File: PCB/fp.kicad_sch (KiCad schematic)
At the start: 29 parts, among them J1 Line Out

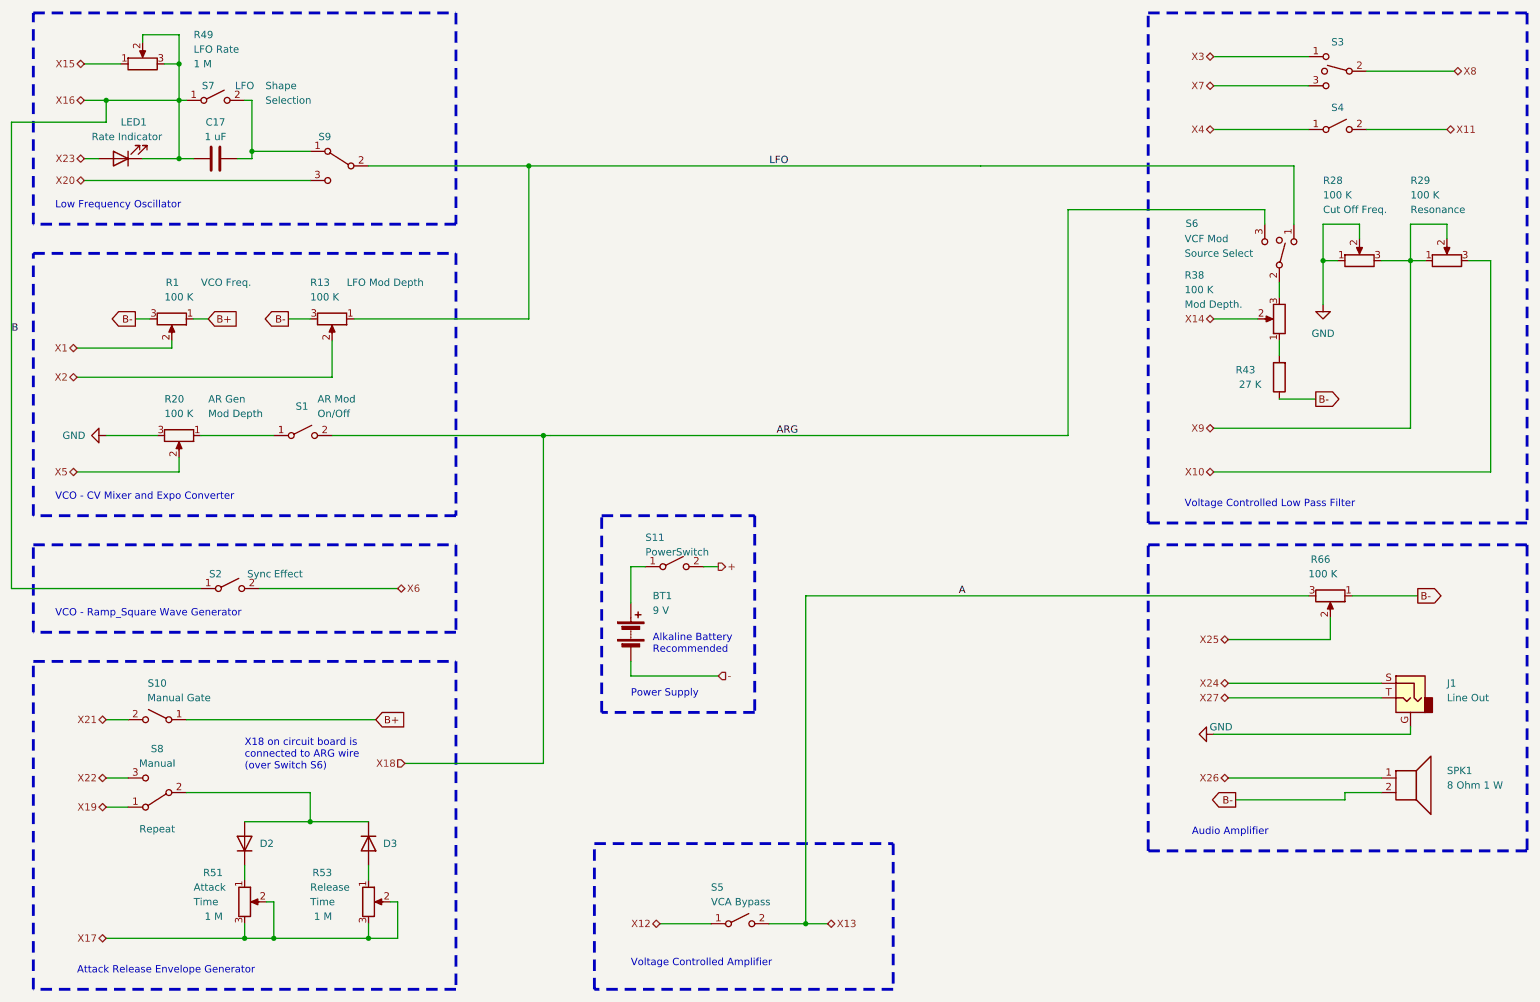
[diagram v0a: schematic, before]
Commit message: Change TO-92 transistors to wide package to avoid shorting during soldering
Added B- hole for speaker
Added more vias to shorten traces
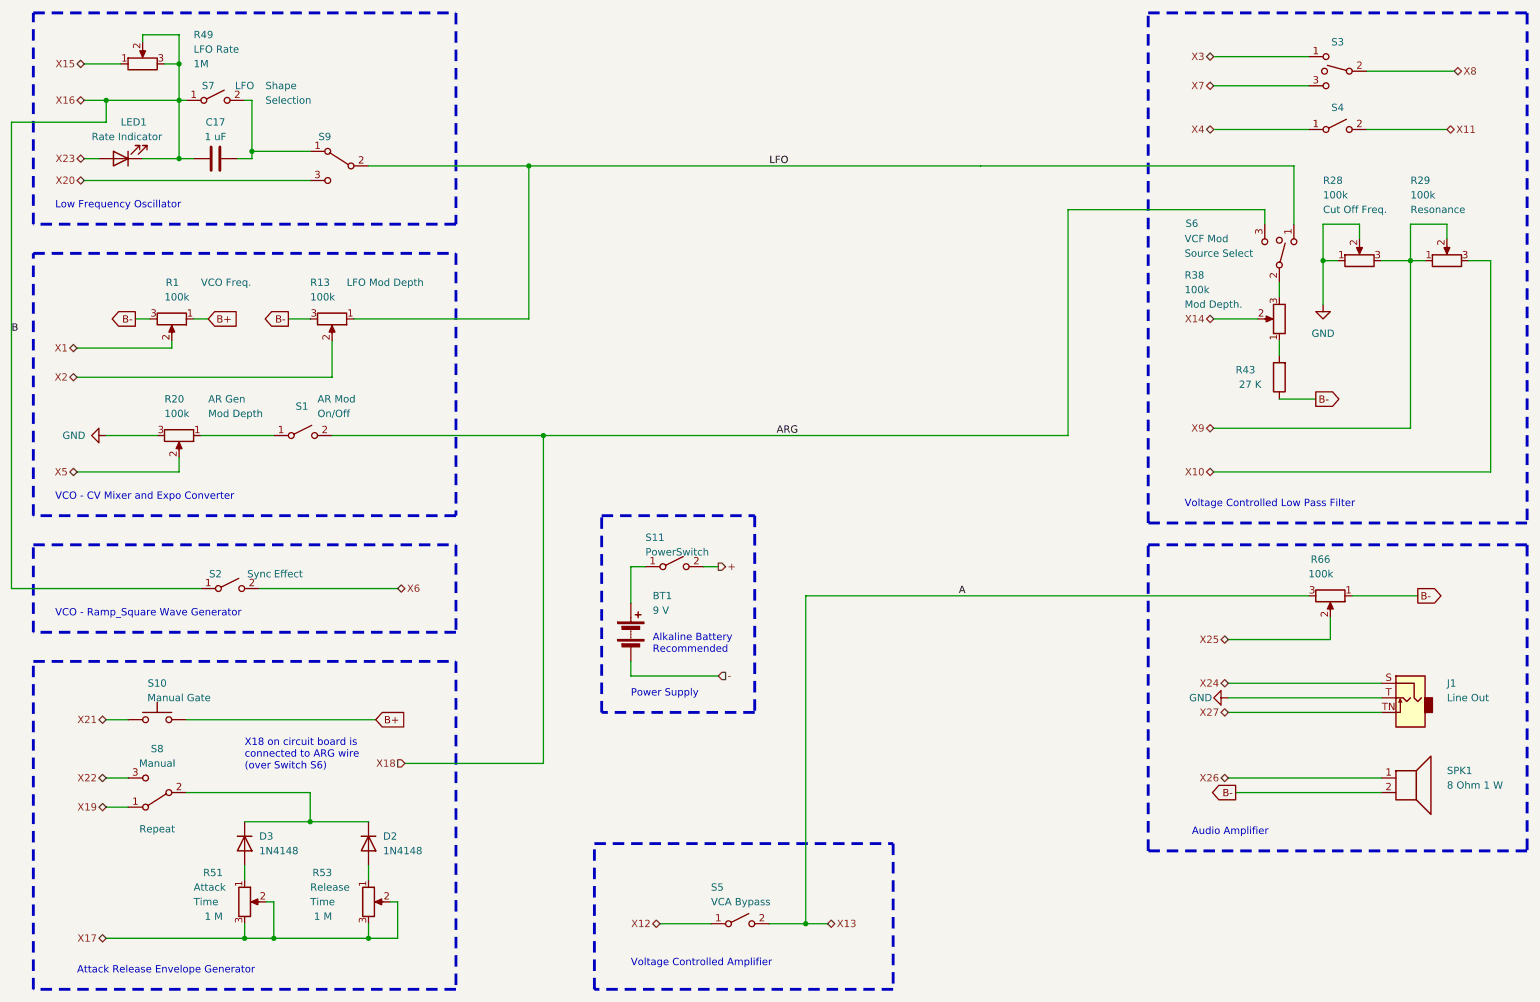
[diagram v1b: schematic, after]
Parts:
- removed D2, D3: D, symbol Device:D
- added D2, D3: 1N4148, Diode_THT:D_DO-35_SOD27_P7.62mm_Horizontal, symbol Diode:1N4148
- J1: symbol Connector_Audio:AudioJack2_Ground -> Connector_Audio:AudioJack2_SwitchT
- R1, R13, R20, R28, R29, R38, R66: value 100 K -> 100k
- R49: value 1 M -> 1M
- S10: symbol Switch:SW_SPST -> Switch:SW_Push
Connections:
- net GND: now also J1.T; no longer J1.G
- net X27: now also J1.TN; no longer J1.T
- net at R51.1: now also D3.2 (A)
- net at S8.2 (B): now also D2.1 (K), D3.1 (K)
- net at R53.1: now also D2.2 (A)

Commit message: whoops
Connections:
- net GND: now also J1.S; no longer J1.T
- net X24: now also J1.T; no longer J1.S
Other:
- note added: "Per Ray`s order, Line Out needs to be a closed jack"
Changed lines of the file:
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@@
 		)
 	)
+	(text "Per Ray`s order, \nLine Out needs to be\na closed jack"
+		(exclude_from_sim no)
+		(at 255.778 126.746 0)
+		(effects
+			(font
+				(size 1.27 1.27)
+			)
+			(justify left)
+		)
+	)
 	(text "VCO - Ramp_Square Wave Generator"
 		(exclude_from_sim no)
@@
 	(wire
 		(pts
-			(xy 228.6 135.89) (xy 255.27 135.89)
+			(xy 228.6 133.35) (xy 255.27 133.35)
 		)
 		(stroke
@@
 	(wire
 		(pts
-			(xy 228.6 133.35) (xy 255.27 133.35)
+			(xy 228.6 135.89) (xy 255.27 135.89)
 		)
 		(stroke
@@
 	(hierarchical_label "X24"
 		(shape bidirectional)
-		(at 228.6 133.35 180)
+		(at 228.6 135.89 180)
 		(effects
 			(font
@@
 	(symbol
 		(lib_id "power:GND")
-		(at 228.6 135.89 270)
+		(at 228.6 133.35 270)
 		(unit 1)
 		(body_style 1)
@@
 		(dnp no)
 		(property "Reference" "#PWR05"
-			(at 222.25 135.89 0)
+			(at 222.25 133.35 0)
 			(hide yes)
 			(show_name no)
@@
 		)
 		(property "Value" "GND"
-			(at 223.774 135.89 90)
+			(at 223.774 133.35 90)
 			(show_name no)
 			(do_not_autoplace no)
@@
 		)
 		(property "Footprint" ""
-			(at 228.6 135.89 0)
+			(at 228.6 133.35 0)
 			(hide yes)
 			(show_name no)
@@
 		)
 		(property "Datasheet" ""
-			(at 228.6 135.89 0)
+			(at 228.6 133.35 0)
 			(hide yes)
 			(show_name no)
@@
 		)
 		(property "Description" ""
-			(at 228.6 135.89 0)
+			(at 228.6 133.35 0)
 			(hide yes)
 			(show_name no)

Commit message: Necessary Changes to Schematic and PCB
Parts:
- removed S9: (no value), symbol Switch:SW_SPDT
- added SW9: SW_SPDT, symbol Switch:SW_SPDT
- S3: value (none) -> SW_SPDT_MSM
- S6: Wert2 Source Select -> (none)
- S8: value Repeat -> Manual; Wert 2 Manual -> (none)
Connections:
- net LFO: now also SW9.2 (B)
- net X20: now also SW9.3 (C)
- net at C17.2, S7.2 (B): now also SW9.1 (A)

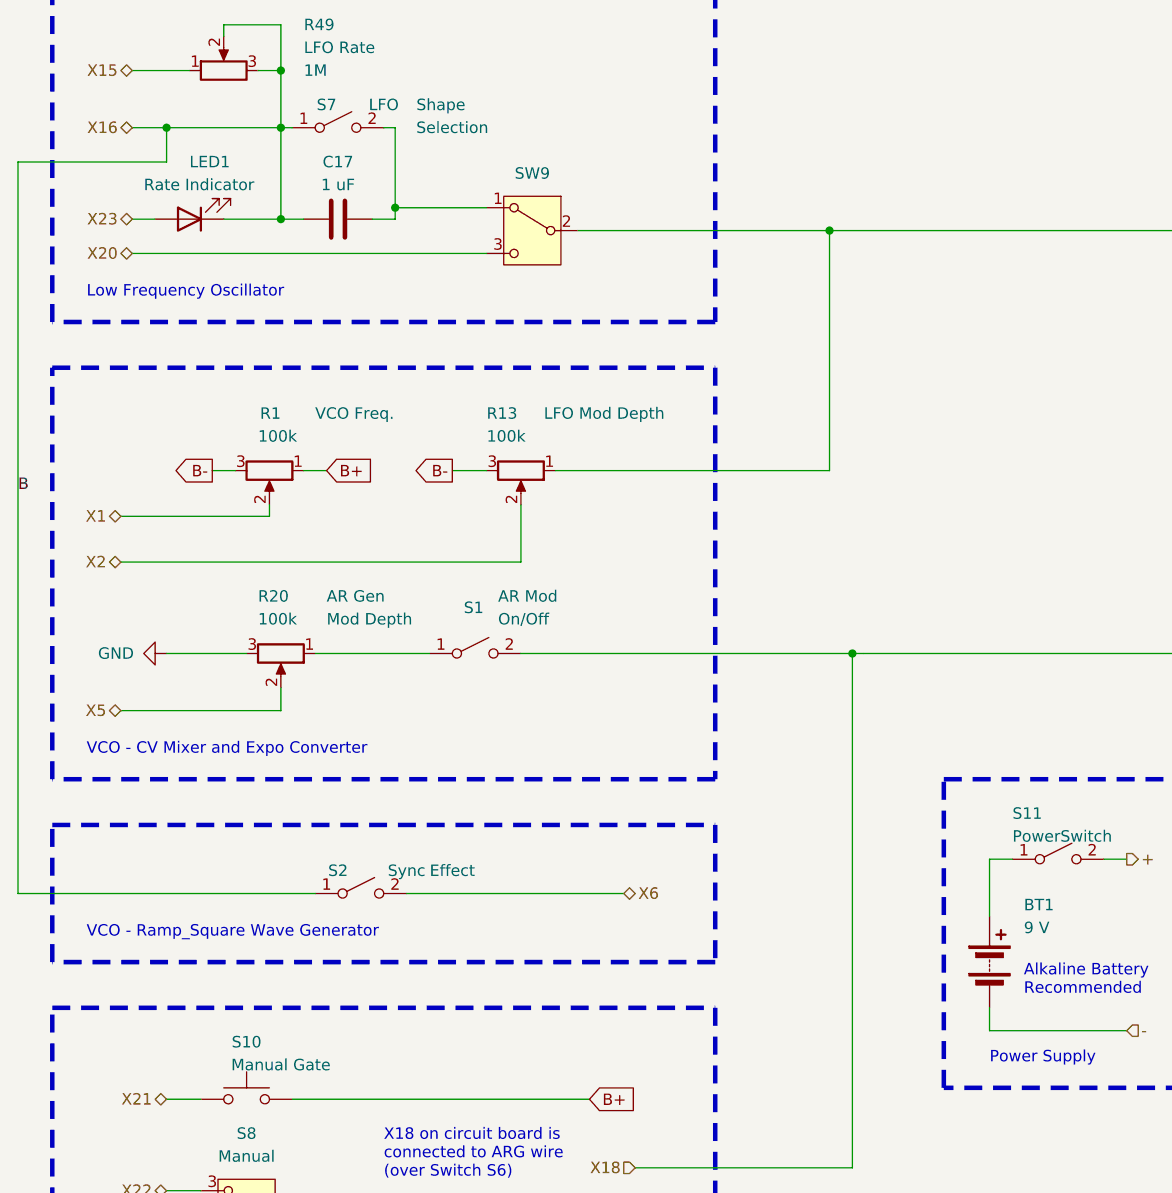
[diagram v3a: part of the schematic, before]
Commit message: Final Update
Move power pins closer to filter caps
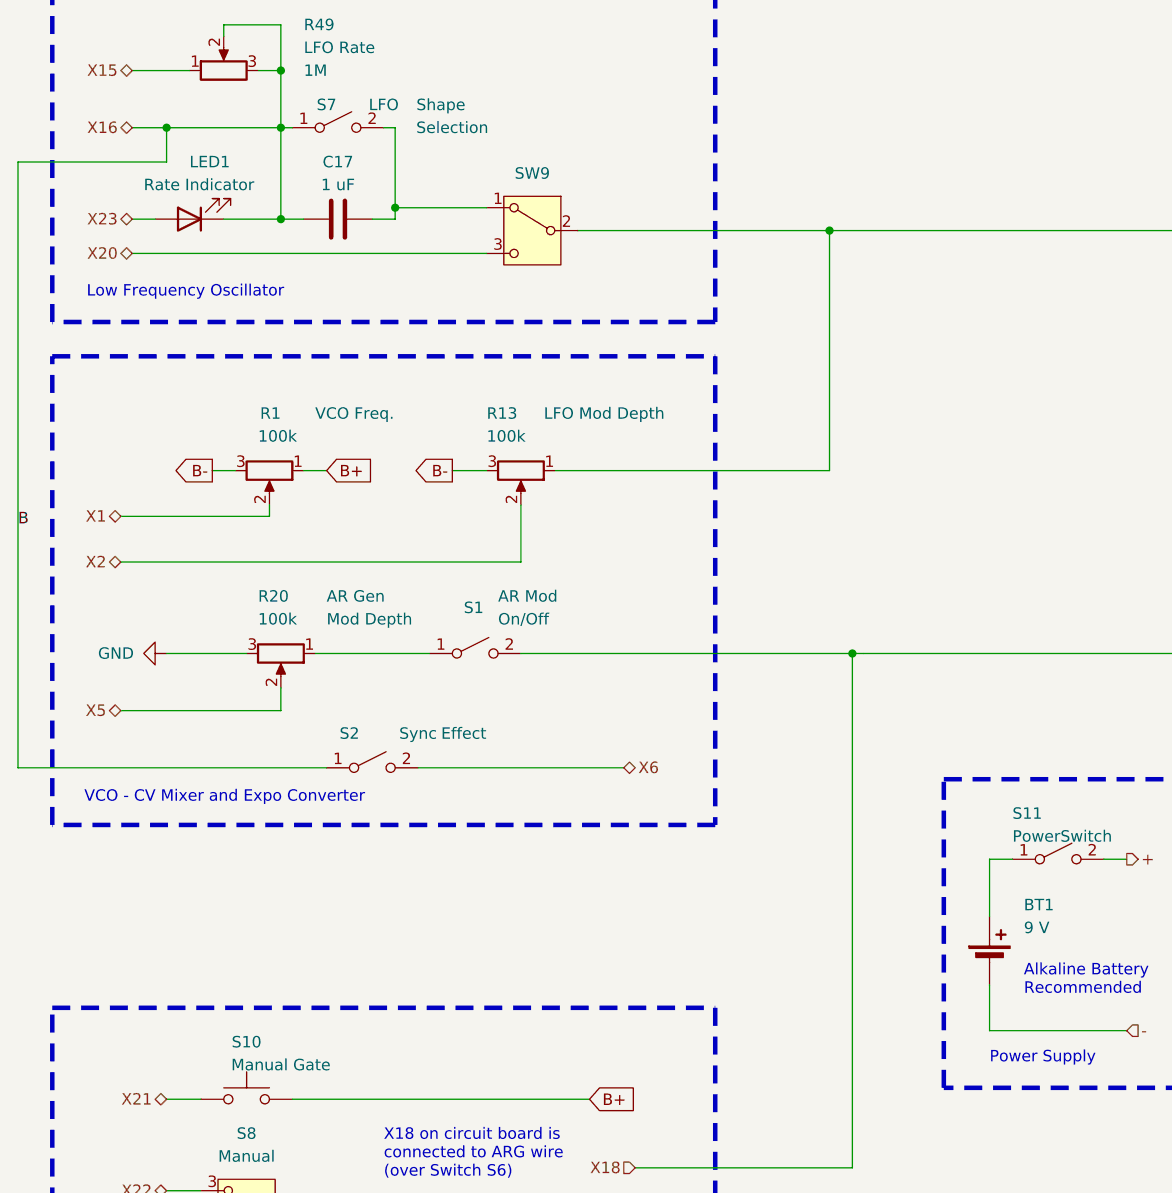
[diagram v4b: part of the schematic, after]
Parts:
- BT1: symbol Device:Battery -> Device:Battery_Cell
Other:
- note removed: "VCO - Ramp_Square Wave Generator"
- moved on the sheet: S2
